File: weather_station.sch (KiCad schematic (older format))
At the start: 73 parts, among them J1 Conn_01x03, J2 Conn_01x05_Male, J3 Conn_01x05, J4 Conn_02x04_Odd_Even, J5 USB_B_Micro, P1 USB_C_Plug, Q1 BSS138, Q2 BSS84, Q3 BSS84, Q4 BSS138_NC, Q5 BSS138, SW1 SW_Push, U1 ESP-12F, U2 AMS1117-3.3, U3 LM75B, U4 BME280, U5 BME680

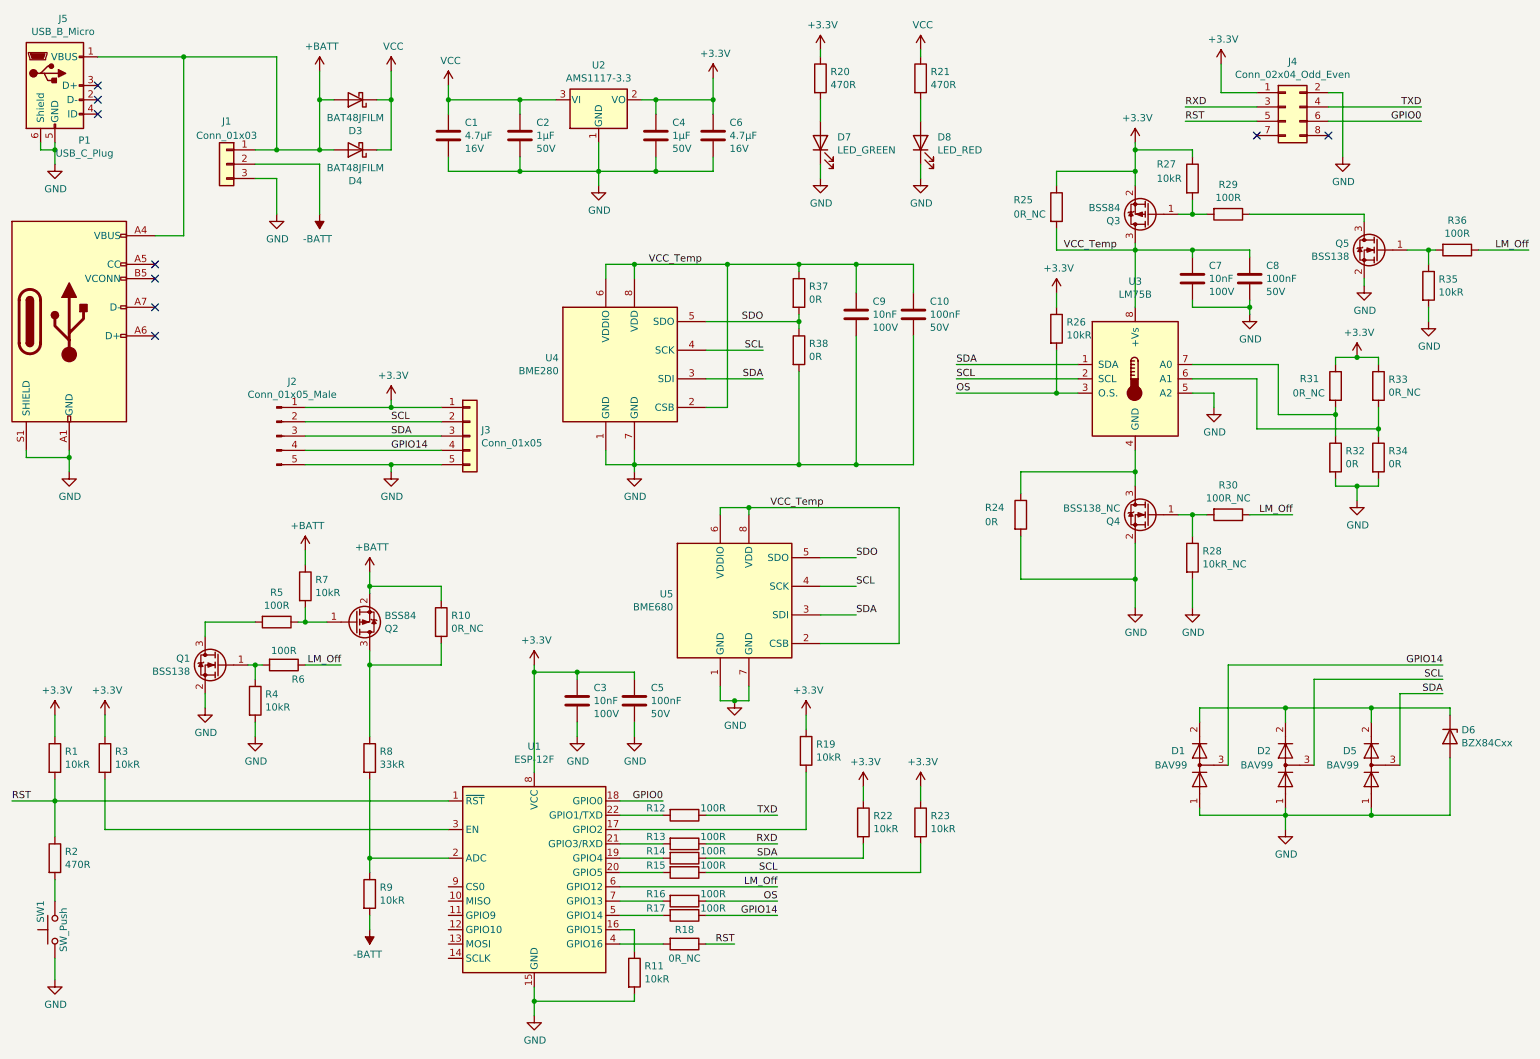
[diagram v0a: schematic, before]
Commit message: Edit NC Components and update footprints
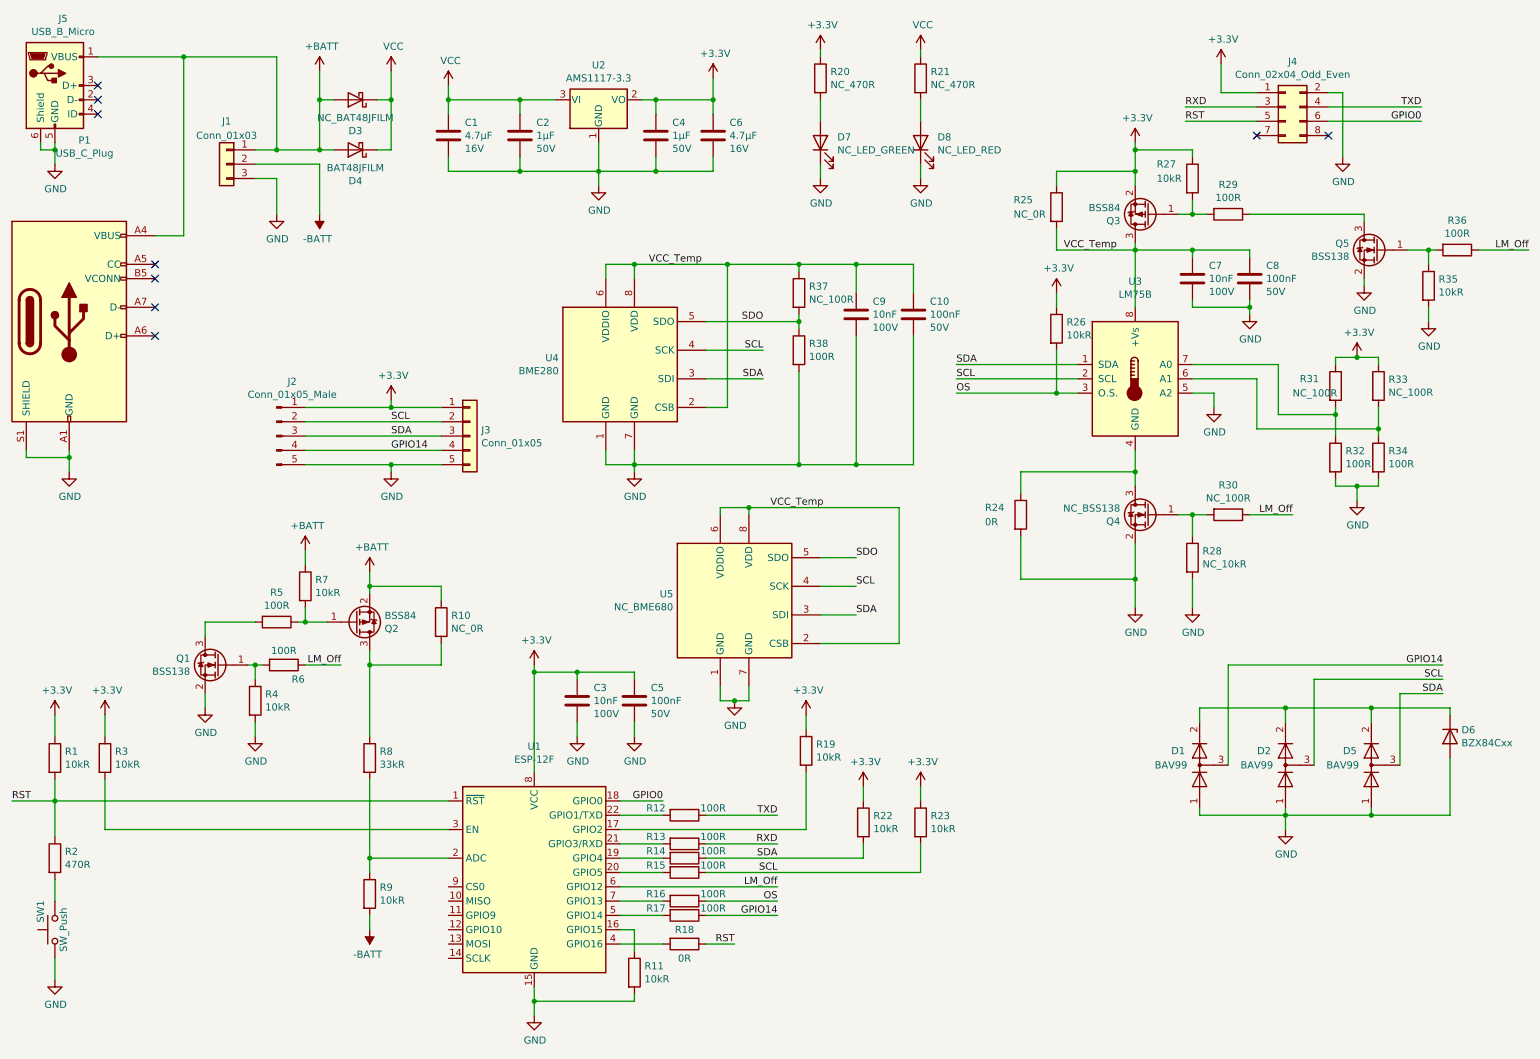
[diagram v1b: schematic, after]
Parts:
- D3: value BAT48JFILM -> NC_BAT48JFILM
- D7: value LED_GREEN -> NC_LED_GREEN
- D8: value LED_RED -> NC_LED_RED
- Q4: value BSS138_NC -> NC_BSS138
- R10, R25: value 0R_NC -> NC_0R
- R18: value 0R_NC -> 0R
- R20, R21: value 470R -> NC_470R
- R28: value 10kR_NC -> NC_10kR
- R30: value 100R_NC -> NC_100R
- R31, R33: value 0R_NC -> NC_100R
- R32, R34, R38: value 0R -> 100R
- R37: value 0R -> NC_100R
- U5: value BME680 -> NC_BME680
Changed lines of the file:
@@
 P 8500 4000
 F 0 "Q4" H 8705 3954 50  0000 L CNN
-F 1 "BSS138_NC" H 8705 4045 50  0000 L CNN
+F 1 "NC_BSS138" H 8705 4045 50  0000 L CNN
 F 2 "Package_TO_SOT_SMD:SOT-23" H 8700 3925 50  0001 L CIN
 F 3 "https://www.onsemi.com/pub/Collateral/BSS138-D.PDF" H 8500 4000 50  0001 L CNN
@@
 P 8800 4300
 F 0 "R28" H 8870 4346 50  0000 L CNN
-F 1 "10kR_NC" H 8870 4255 50  0000 L CNN
+F 1 "NC_10kR" H 8870 4255 50  0000 L CNN
 F 2 "Resistor_SMD:R_0805_2012Metric" V 8730 4300 50  0001 C CNN
 F 3 "~" H 8800 4300 50  0001 C CNN
@@
 P 7850 1850
 F 0 "R25" H 7550 1900 50  0000 L CNN
-F 1 "0R_NC" H 7550 1800 50  0000 L CNN
+F 1 "NC_0R" H 7550 1800 50  0000 L CNN
 F 2 "Resistor_SMD:R_0805_2012Metric" V 7780 1850 50  0001 C CNN
 F 3 "~" H 7850 1850 50  0001 C CNN
@@
 P 9050 4000
 F 0 "R30" V 8843 4000 50  0000 C CNN
-F 1 "100R_NC" V 8934 4000 50  0000 C CNN
+F 1 "NC_100R" V 8934 4000 50  0000 C CNN
 F 2 "Resistor_SMD:R_0805_2012Metric" V 8980 4000 50  0001 C CNN
 F 3 "~" H 9050 4000 50  0001 C CNN
@@
 P 6900 950
 F 0 "R21" H 6970 996 50  0000 L CNN
-F 1 "470R" H 6970 905 50  0000 L CNN
+F 1 "NC_470R" H 6970 905 50  0000 L CNN
 F 2 "Resistor_SMD:R_0805_2012Metric" V 6830 950 50  0001 C CNN
 F 3 "~" H 6900 950 50  0001 C CNN
@@
 P 6900 1400
 F 0 "D8" V 6939 1282 50  0000 R CNN
-F 1 "LED_RED" V 6848 1282 50  0000 R CNN
+F 1 "NC_LED_RED" V 6848 1282 50  0000 R CNN
 F 2 "LED_SMD:LED_0805_2012Metric" H 6900 1400 50  0001 C CNN
 F 3 "~" H 6900 1400 50  0001 C CNN
@@
 P 5250 7000
 F 0 "R18" V 5150 7000 50  0000 C CNN
-F 1 "0R_NC" V 5350 7000 50  0000 C CNN
+F 1 "0R" V 5350 7000 50  0000 C CNN
 F 2 "Resistor_SMD:R_0805_2012Metric" V 5180 7000 50  0001 C CNN
 F 3 "~" H 5250 7000 50  0001 C CNN
@@
 P 2950 1100
 F 0 "D3" H 2950 1317 50  0000 C CNN
-F 1 "BAT48JFILM" H 2950 1226 50  0000 C CNN
+F 1 "NC_BAT48JFILM" H 2950 1226 50  0000 C CNN
 F 2 "Diode_SMD:D_SOD-323" H 2950 925 50  0001 C CNN
 F 3 "www.st.com/resource/en/datasheet/bat48.pdf" H 2950 1100 50  0001 C CNN
@@
 P 6200 950
 F 0 "R20" H 6270 996 50  0000 L CNN
-F 1 "470R" H 6270 905 50  0000 L CNN
+F 1 "NC_470R" H 6270 905 50  0000 L CNN
 F 2 "Resistor_SMD:R_0805_2012Metric" V 6130 950 50  0001 C CNN
 F 3 "~" H 6200 950 50  0001 C CNN
@@
 P 6200 1400
 F 0 "D7" V 6239 1282 50  0000 R CNN
-F 1 "LED_GREEN" V 6148 1282 50  0000 R CNN
+F 1 "NC_LED_GREEN" V 6148 1282 50  0000 R CNN
 F 2 "LED_SMD:LED_0805_2012Metric" H 6200 1400 50  0001 C CNN
 F 3 "~" H 6200 1400 50  0001 C CNN
@@
 P 3550 4750
 F 0 "R10" H 3620 4796 50  0000 L CNN
-F 1 "0R_NC" H 3620 4705 50  0000 L CNN
+F 1 "NC_0R" H 3620 4705 50  0000 L CNN
 F 2 "Resistor_SMD:R_0805_2012Metric" V 3480 4750 50  0001 C CNN
 F 3 "~" H 3550 4750 50  0001 C CNN
@@
 P 9800 3100
 F 0 "R31" H 9550 3150 50  0000 L CNN
-F 1 "0R_NC" H 9500 3050 50  0000 L CNN
+F 1 "NC_100R" H 9500 3050 50  0000 L CNN
 F 2 "Resistor_SMD:R_0805_2012Metric" V 9730 3100 50  0001 C CNN
 F 3 "~" H 9800 3100 50  0001 C CNN
@@
 P 10100 3100
 F 0 "R33" H 10170 3146 50  0000 L CNN
-F 1 "0R_NC" H 10170 3055 50  0000 L CNN
+F 1 "NC_100R" H 10170 3055 50  0000 L CNN
 F 2 "Resistor_SMD:R_0805_2012Metric" V 10030 3100 50  0001 C CNN
 F 3 "~" H 10100 3100 50  0001 C CNN
@@
 P 9800 3600
 F 0 "R32" H 9870 3646 50  0000 L CNN
-F 1 "0R" H 9870 3555 50  0000 L CNN
+F 1 "100R" H 9870 3555 50  0000 L CNN
 F 2 "Resistor_SMD:R_0805_2012Metric" V 9730 3600 50  0001 C CNN
 F 3 "~" H 9800 3600 50  0001 C CNN
@@
 P 10100 3600
 F 0 "R34" H 10170 3646 50  0000 L CNN
-F 1 "0R" H 10170 3555 50  0000 L CNN
+F 1 "100R" H 10170 3555 50  0000 L CNN
 F 2 "Resistor_SMD:R_0805_2012Metric" V 10030 3600 50  0001 C CNN
 F 3 "~" H 10100 3600 50  0001 C CNN
@@
 P 5600 4600
 F 0 "U5" H 5171 4646 50  0000 R CNN
-F 1 "BME680" H 5171 4555 50  0000 R CNN
+F 1 "NC_BME680" H 5171 4555 50  0000 R CNN
 F 2 "Package_LGA:Bosch_LGA-8_3x3mm_P0.8mm_ClockwisePinNumbering" H 7050 4150 50  0001 C CNN
 F 3 "https://ae-bst.resource.bosch.com/media/_tech/media/datasheets/BST-BME680-DS001.pdf" H 5600 4400 50  0001 C CNN
@@
 P 6050 2450
 F 0 "R37" H 6120 2496 50  0000 L CNN
-F 1 "0R" H 6120 2405 50  0000 L CNN
+F 1 "NC_100R" H 6120 2405 50  0000 L CNN
 F 2 "Resistor_SMD:R_0805_2012Metric" V 5980 2450 50  0001 C CNN
 F 3 "~" H 6050 2450 50  0001 C CNN
@@
 P 6050 2850
 F 0 "R38" H 6120 2896 50  0000 L CNN
-F 1 "0R" H 6120 2805 50  0000 L CNN
+F 1 "100R" H 6120 2805 50  0000 L CNN
 F 2 "Resistor_SMD:R_0805_2012Metric" V 5980 2850 50  0001 C CNN
 F 3 "~" H 6050 2850 50  0001 C CNN
